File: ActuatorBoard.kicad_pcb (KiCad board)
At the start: 2 copper layers, 75 x 89.5 mm, 39 parts, among them J1 CONN_02X04, J2 Screw_Terminal_01x02, J3 Screw_Terminal_01x02, J4 CONN_02X04, J5 CONN_01X03, M1 Aktuator_Module, M2 Aktuator_Module, M3 Aktuator_Module, M4 Aktuator_Module, M5 Aktuator_Module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

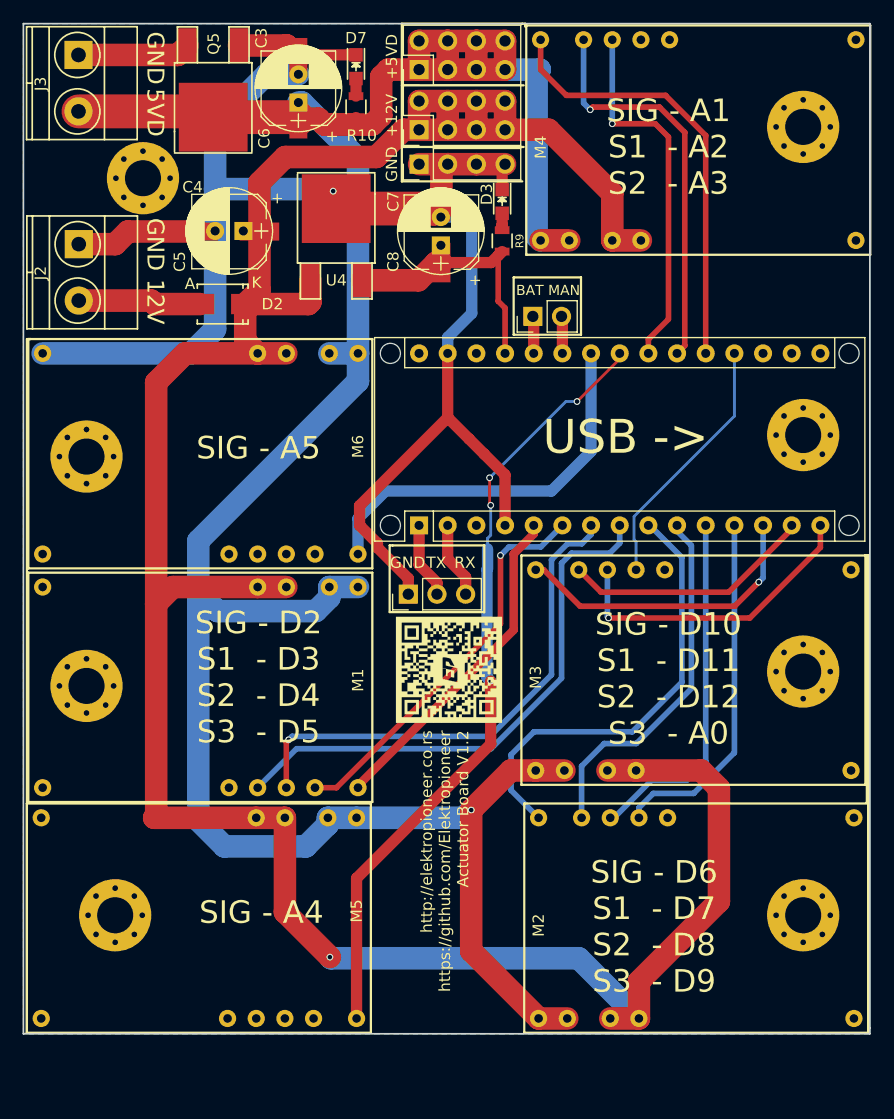
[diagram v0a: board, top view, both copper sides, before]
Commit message: Changed position of two pins because of future h bridge pwm requirements
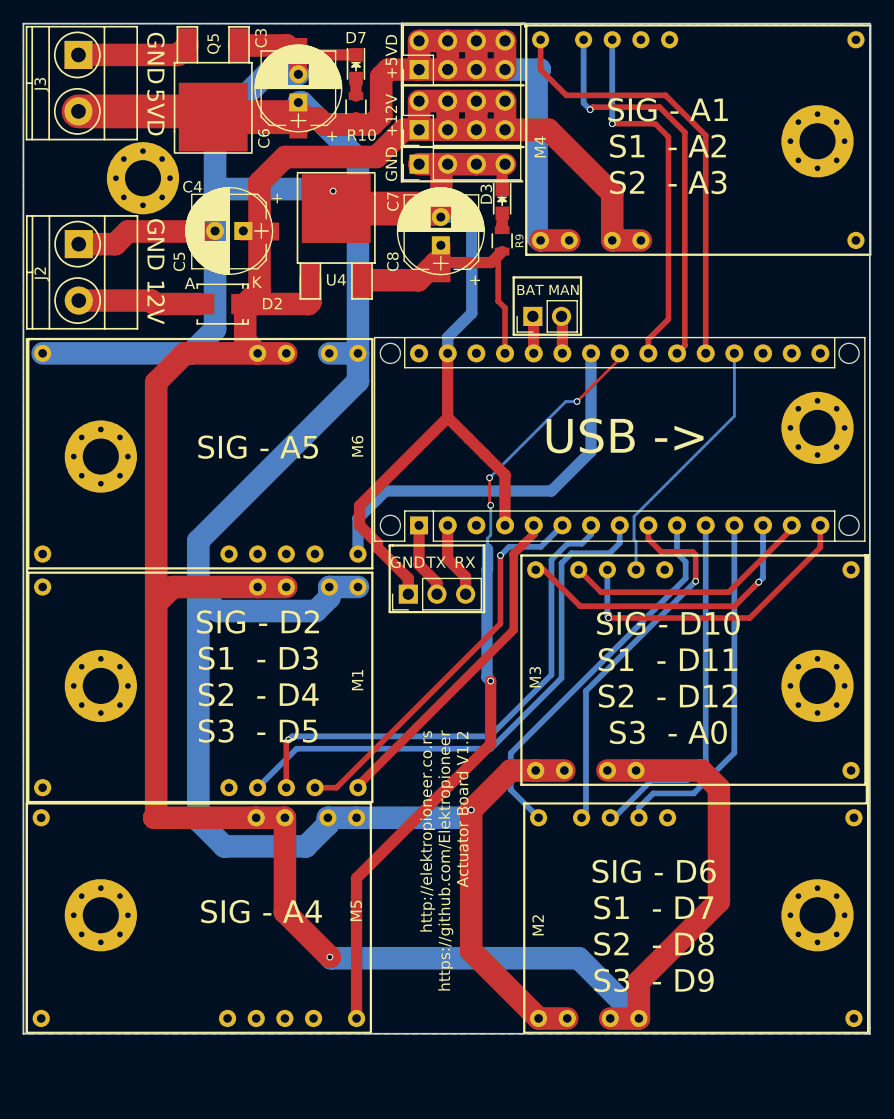
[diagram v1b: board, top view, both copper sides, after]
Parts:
- removed the G*** at (199.2, 81.8)
- removed REF***: KiCad-Logo2_12mm_SilkScreen, Symbols:KiCad-Logo2_12mm_SilkScreen
- moved G*** 37.7 mm to (220.0, 81.0)
- moved G*** 19.5 mm to (185.9, 63.0)
- moved MK3 1.80 mm to (231.9, 83.2)
- moved MK7 1.80 mm to (231.9, 34.9)
- moved MK8 1.42 mm to (231.9, 60.3)
- moved MK2 1.27 mm to (231.9, 103.5)
- moved MK5 1.27 mm to (168.4, 83.2)
- moved MK6 1.27 mm to (168.4, 62.9)
- moved MK4 1.27 mm to (168.4, 103.5)
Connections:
- M2 pad 3: SIG5 -> SIG6
- M2 pad 6: SIG6 -> SIG5
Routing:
- net SIG5: track 39.6 -> 33.6 mm, vias 0 -> 1
- net SIG6: track 32.1 -> 34.2 mm

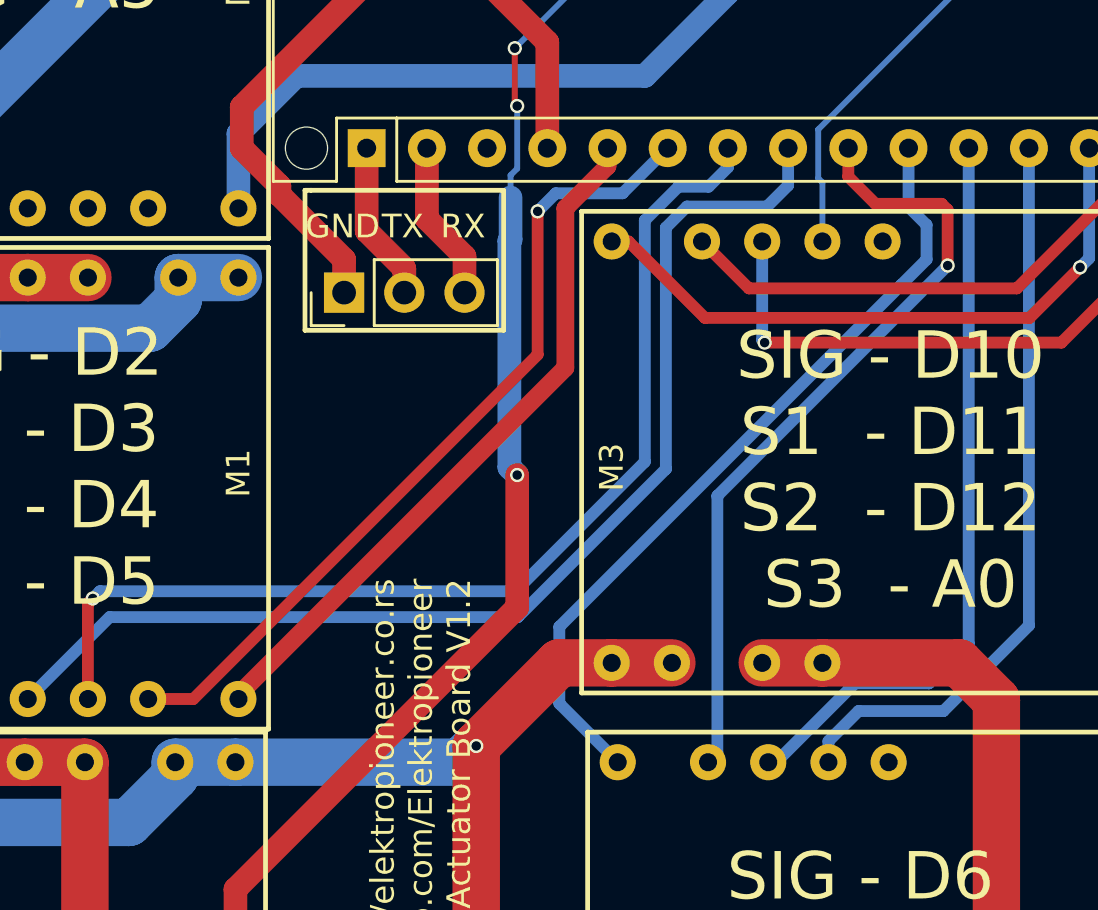
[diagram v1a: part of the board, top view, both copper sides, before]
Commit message: Added actuator board drill and gerber
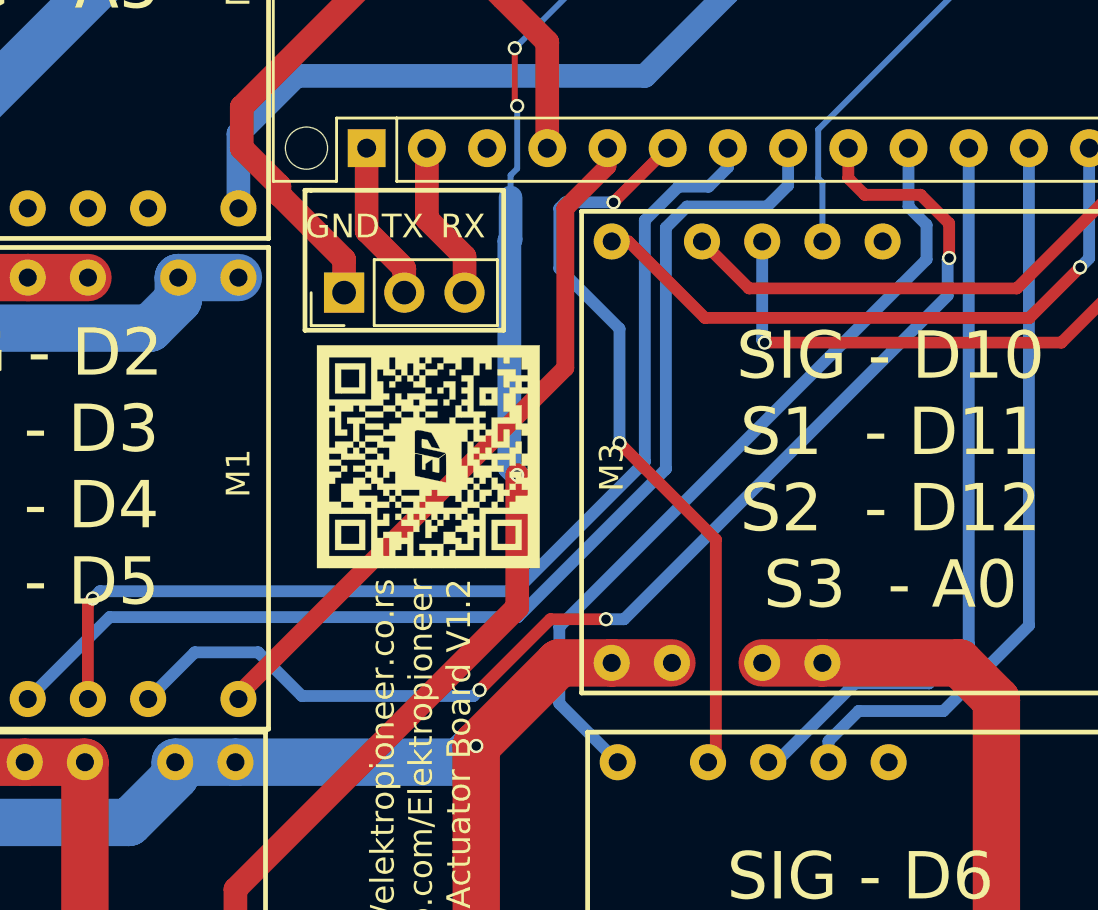
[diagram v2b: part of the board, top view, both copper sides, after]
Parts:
- added G***: LOGO, Hardware:EP_Logo, F.Cu at (199.2, 82.0)
- moved G*** 37.5 mm to (225.3, 43.9)
- moved G*** 24.0 mm to (199.0, 83.1)
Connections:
- M1 pad 6: SIG2 -> SIG5
- M2 pad 6: SIG5 -> SIG2
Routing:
- net SIG5: track 33.6 -> 51.8 mm, vias 1 -> 3
- net SIG2: track 35.1 -> 32.4 mm, vias 1 -> 2
